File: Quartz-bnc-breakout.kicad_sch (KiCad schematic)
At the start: 27 parts, among them J1 Conn_Coaxial, J10 Conn_Coaxial, J11 Conn_Coaxial, J12 Conn_Coaxial, J13 Conn_Coaxial, J14 Conn_Coaxial, J15 Conn_Coaxial, J16 Conn_Coaxial, J17 DC37_Pins_MountingHoles, J2 Conn_Coaxial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

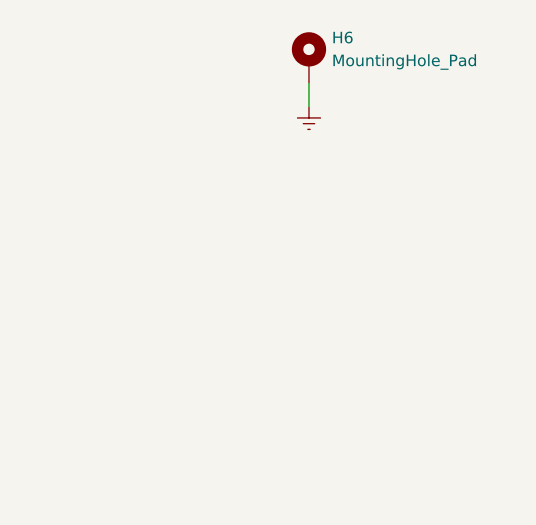
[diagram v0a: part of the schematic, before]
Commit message: Changed mounting hole footprints from 3mm to 3.4mm
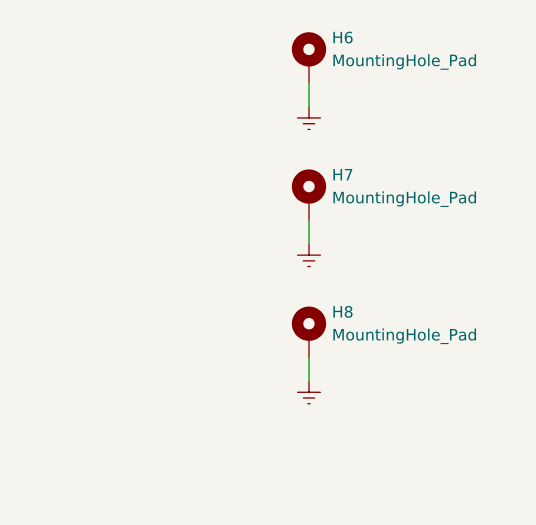
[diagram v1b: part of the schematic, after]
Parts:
- added H7, H8: MountingHole_Pad, 0local:MountingHole_3.4mm_Pad, symbol 0local:MountingHole_Pad
- H1, H2, H3, H4, H5, H6: footprint 0local:MountingHole_3mm_Pad -> 0local:MountingHole_3.4mm_Pad
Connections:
- net Earth: now also H7.1, H8.1
